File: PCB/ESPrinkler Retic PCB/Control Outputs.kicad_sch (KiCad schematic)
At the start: 117 parts, among them Q10 AO3400A, Q11 AO3400A, Q3 AO3400A, Q4 AO3400A, Q5 AO3400A, Q6 AO3400A, Q7 AO3400A, Q8 AO3400A, Q9 AO3400A, U10 MOC3063S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

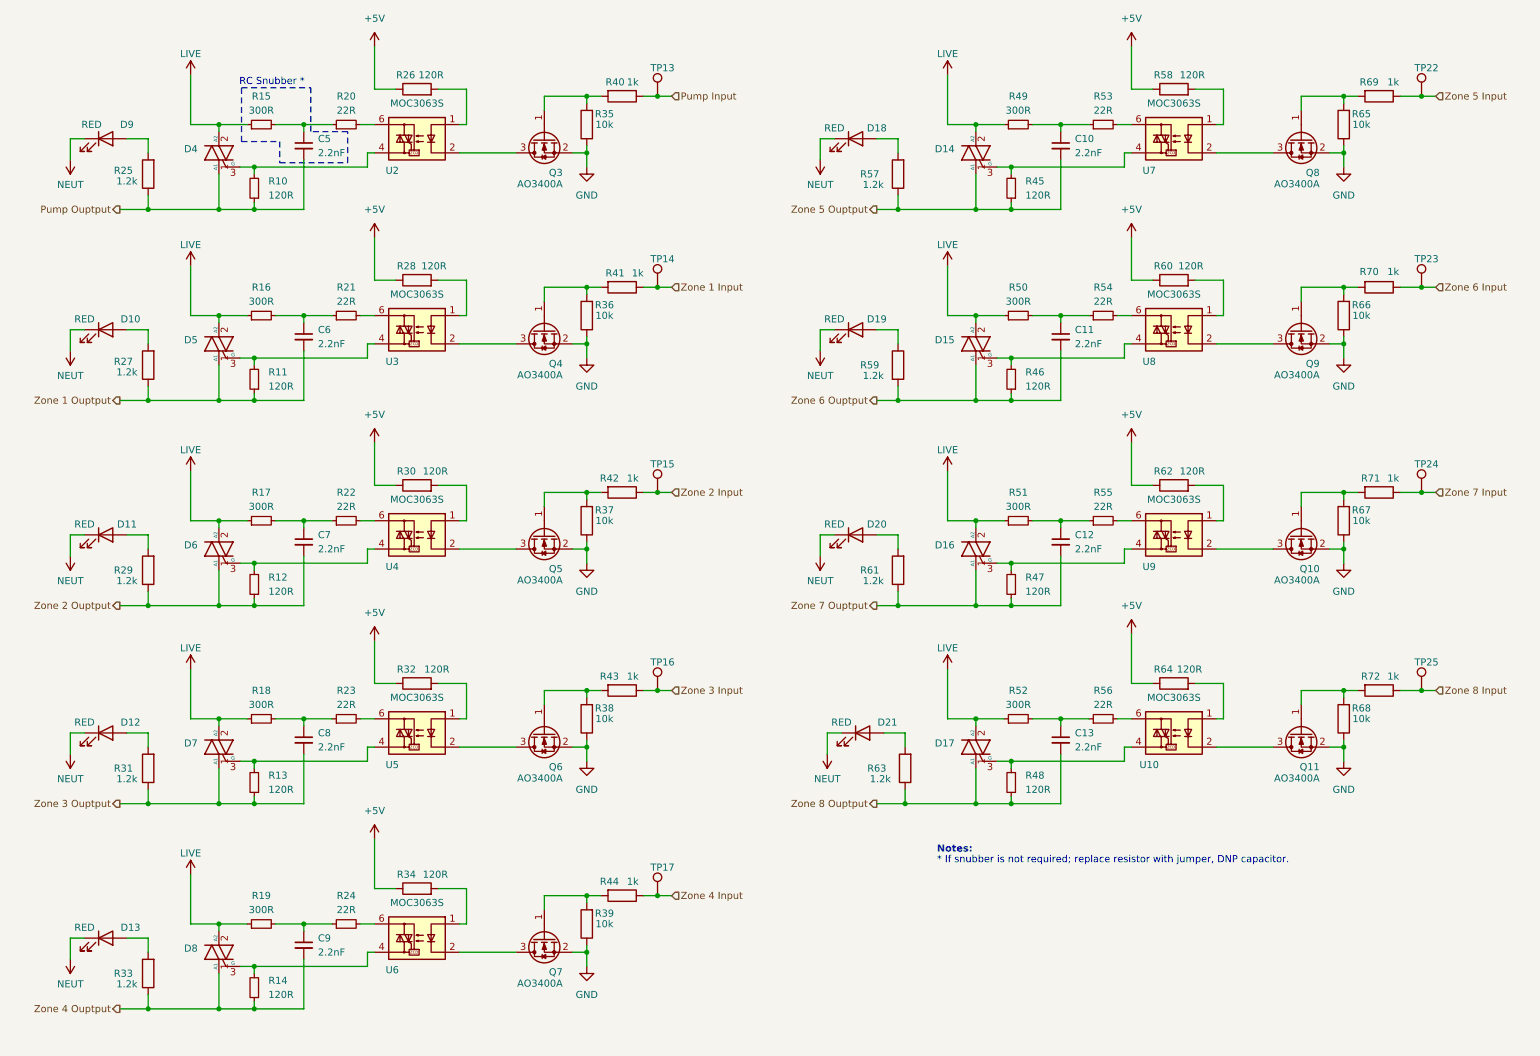
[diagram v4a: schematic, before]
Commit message: PCB version 1.1 following peer review
PTC in line with live, previously shorted between live and neutral.
Added boxes around sections on schematic for better readability.
Modified terminal block silkscreen to make more sense
Modified routing of 5V power to to reduce tunnels and traces on bottom plane.
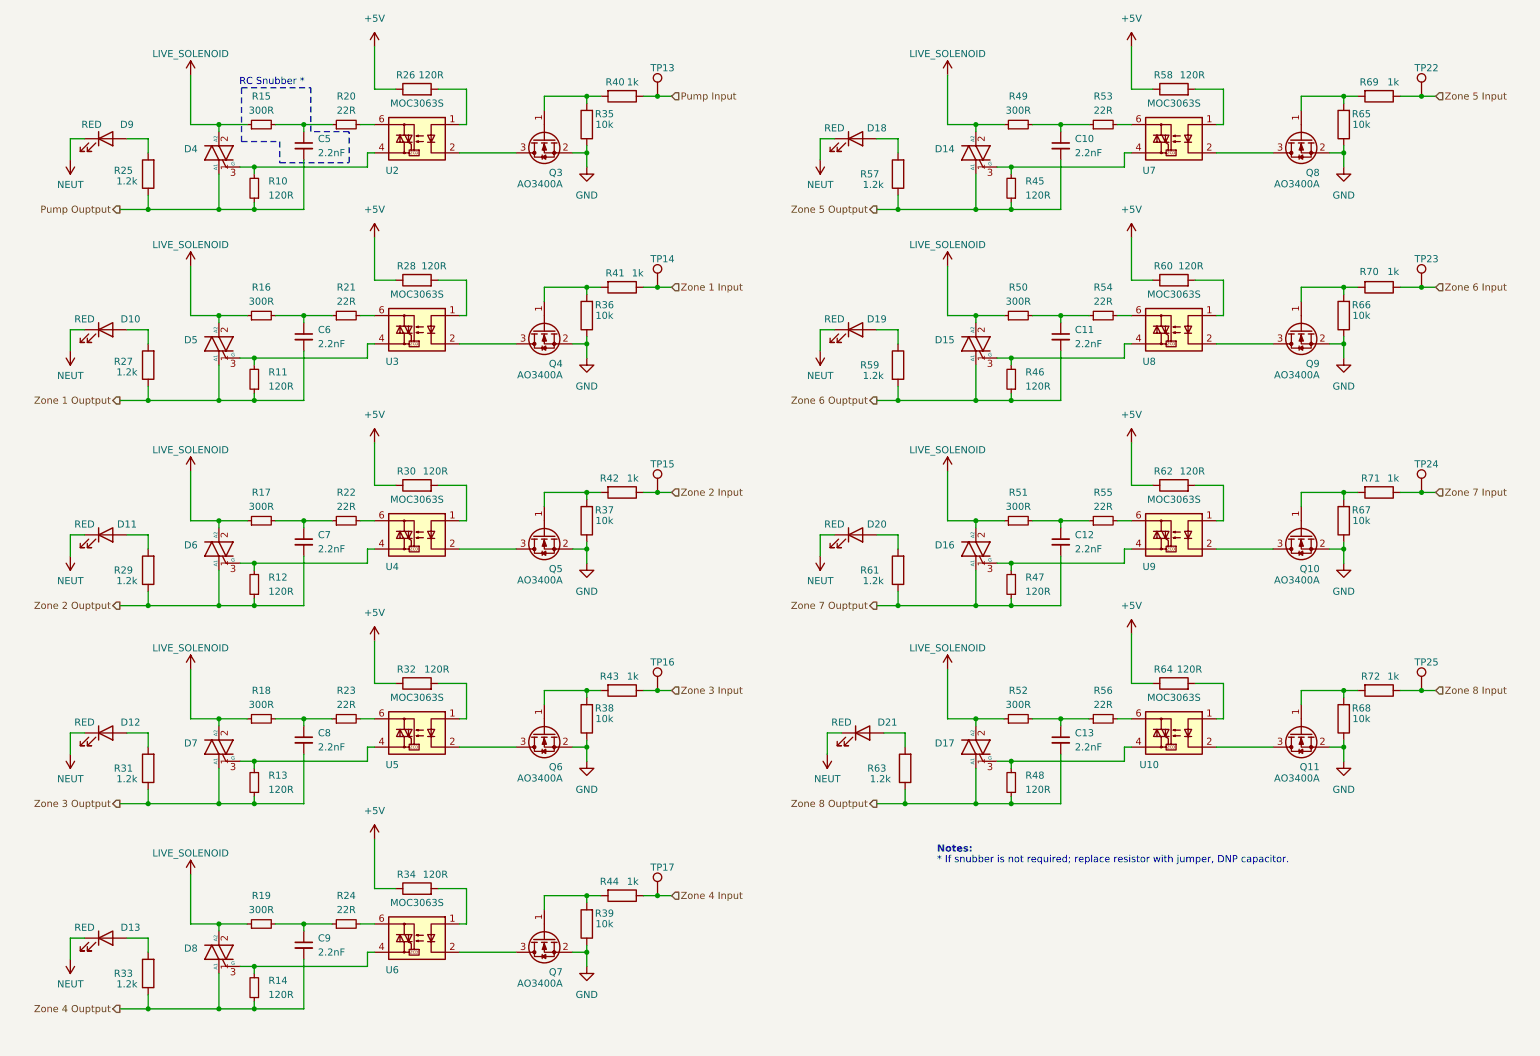
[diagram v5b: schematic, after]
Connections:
- net LIVE renamed LIVE_SOLENOID

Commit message: Continue V1.1 modifications
Round off corners on PCB
Remove solder mount for triacs, unnecessary addition. Can use adhesive if required to secure triacs.
Remove unnecessary vias between top and bottom ground planes
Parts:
- D14, D15, D16, D17, D4, D5, D6, D7, D8: footprint Footprints:TO-220-3_Horizontal_TabDown_Solder -> Footprints:TO-220-3_Horizontal_TabDown_NoHole
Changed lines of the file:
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@@
 			)
 		)
-		(property "Footprint" "Footprints:TO-220-3_Horizontal_TabDown_Solder"
+		(property "Footprint" "Footprints:TO-220-3_Horizontal_TabDown_NoHole"
 			(at 182.245 71.755 90)
 			(effects
@@
 			)
 		)
-		(property "Footprint" "Footprints:TO-220-3_Horizontal_TabDown_Solder"
+		(property "Footprint" "Footprints:TO-220-3_Horizontal_TabDown_NoHole"
 			(at 182.245 108.585 90)
 			(effects
@@
 			)
 		)
-		(property "Footprint" "Footprints:TO-220-3_Horizontal_TabDown_Solder"
+		(property "Footprint" "Footprints:TO-220-3_Horizontal_TabDown_NoHole"
 			(at 46.355 108.585 90)
 			(effects
@@
 			)
 		)
-		(property "Footprint" "Footprints:TO-220-3_Horizontal_TabDown_Solder"
+		(property "Footprint" "Footprints:TO-220-3_Horizontal_TabDown_NoHole"
 			(at 46.355 71.755 90)
 			(effects
@@
 			)
 		)
-		(property "Footprint" "Footprints:TO-220-3_Horizontal_TabDown_Solder"
+		(property "Footprint" "Footprints:TO-220-3_Horizontal_TabDown_NoHole"
 			(at 46.355 37.465 90)
 			(effects
@@
 			)
 		)
-		(property "Footprint" "Footprints:TO-220-3_Horizontal_TabDown_Solder"
+		(property "Footprint" "Footprints:TO-220-3_Horizontal_TabDown_NoHole"
 			(at 46.355 144.145 90)
 			(effects
@@
 			)
 		)
-		(property "Footprint" "Footprints:TO-220-3_Horizontal_TabDown_Solder"
+		(property "Footprint" "Footprints:TO-220-3_Horizontal_TabDown_NoHole"
 			(at 46.355 180.975 90)
 			(effects
@@
 			)
 		)
-		(property "Footprint" "Footprints:TO-220-3_Horizontal_TabDown_Solder"
+		(property "Footprint" "Footprints:TO-220-3_Horizontal_TabDown_NoHole"
 			(at 182.245 144.145 90)
 			(effects
@@
 			)
 		)
-		(property "Footprint" "Footprints:TO-220-3_Horizontal_TabDown_Solder"
+		(property "Footprint" "Footprints:TO-220-3_Horizontal_TabDown_NoHole"
 			(at 182.245 37.465 90)
 			(effects

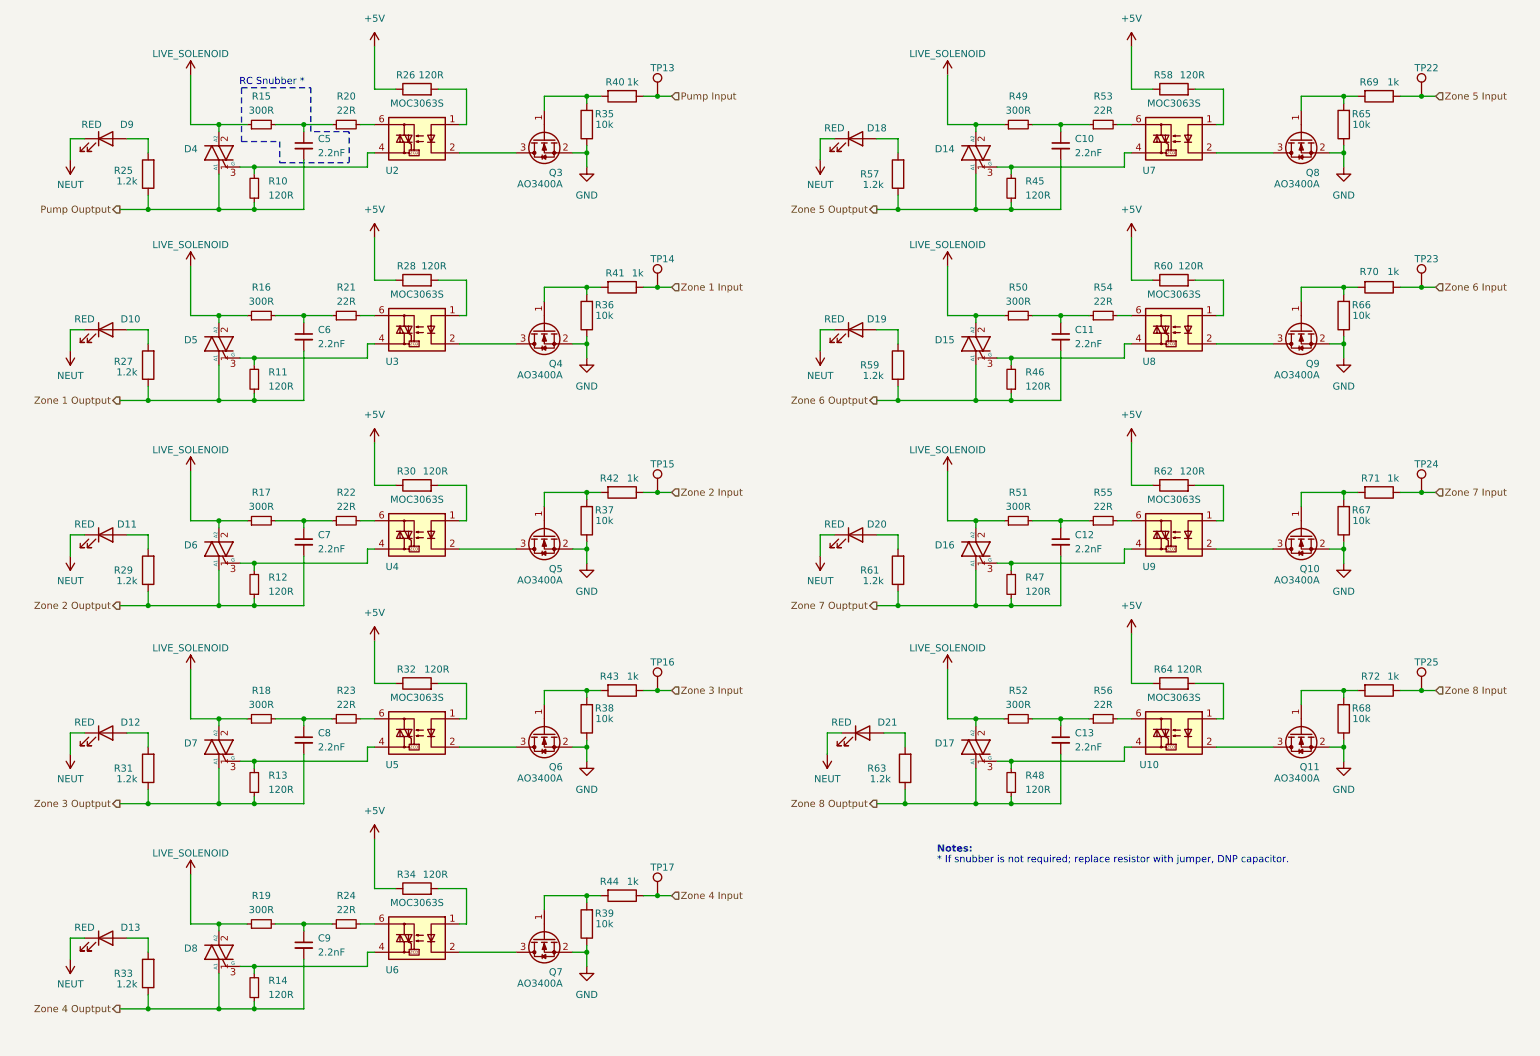
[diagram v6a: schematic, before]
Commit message: Update PCB and SCH for snubber circuit DNF
Snubber circuit is drawing too much power, capacitor and resistor values need to be looked at.
Not including the circuit for the time being.

Added alternate part for resistor, 0 ohm jumper.
DNF capacitor in snubber circuit for each output.
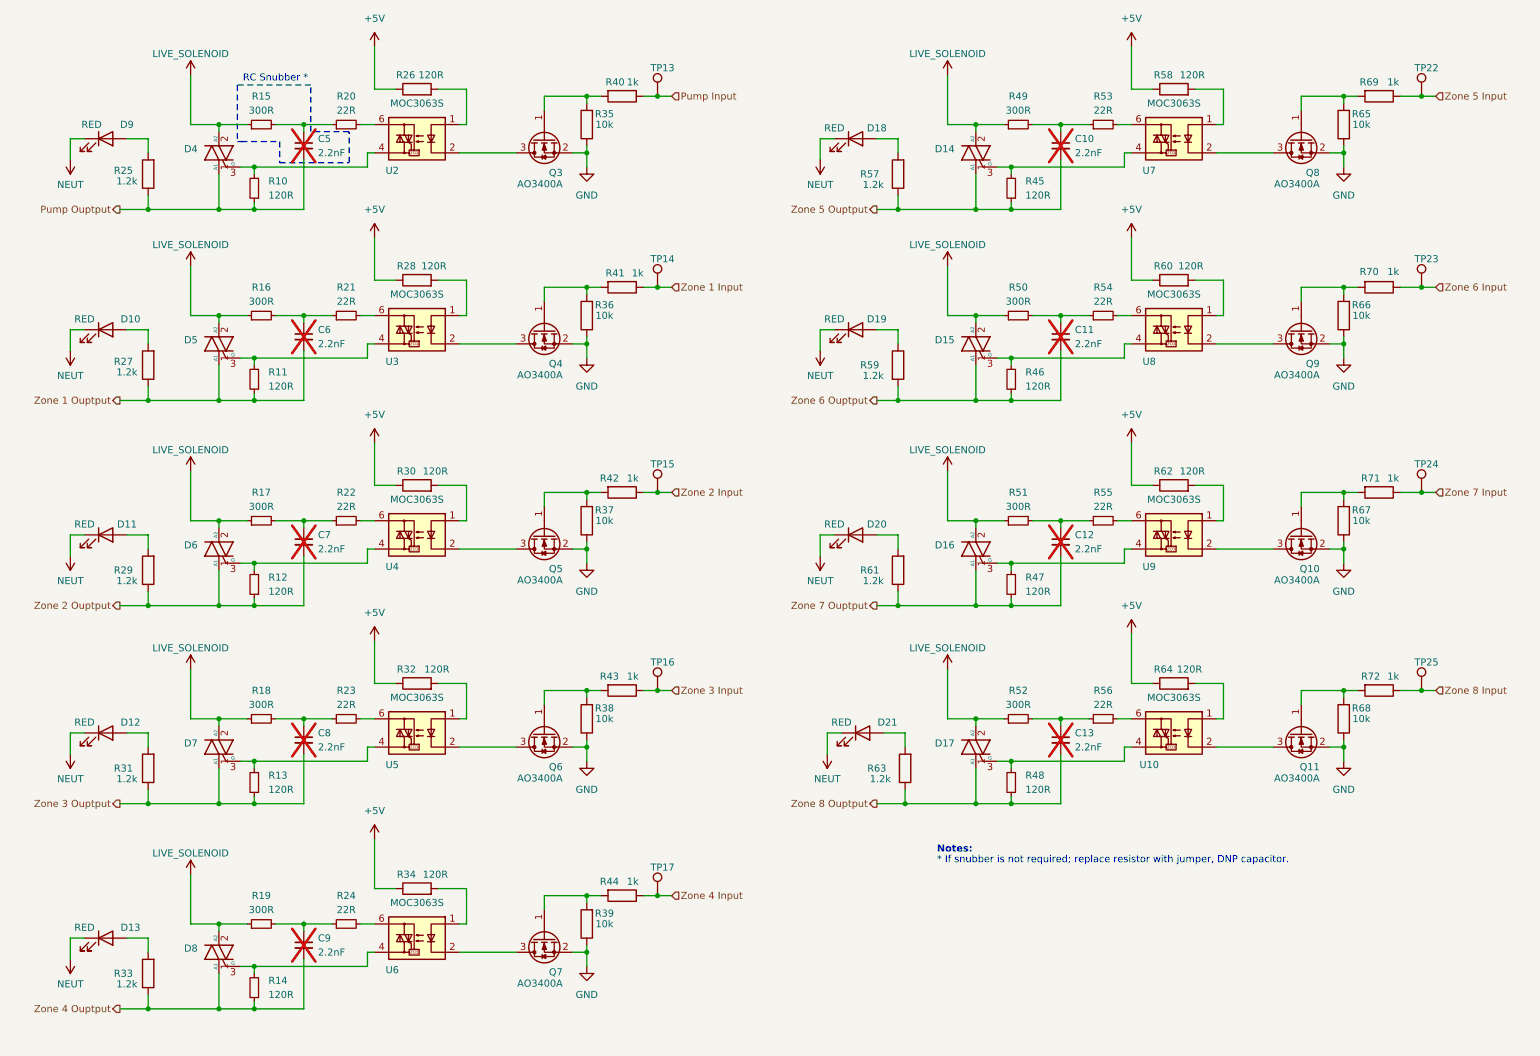
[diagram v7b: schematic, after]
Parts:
- C10, C11, C12, C13, C5, C6, C7, C8, C9: now not fitted
- R15, R16, R17, R18, R19, R49, R50, R51, R52: Alternate Manufacturer (none) -> UNI-ROYAL(Uniroyal Elec); Alternate Manufacturer P/N (none) -> 0805W8F0000T5E; Alternate Supplier (none) -> LCSC; Alternate Supplier P/N (none) -> C17477

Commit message: Remove snubber and bring Kicad V10 update
Remove snubber from triac driver as its not required.

Attempt to start migrating to Kicad V10
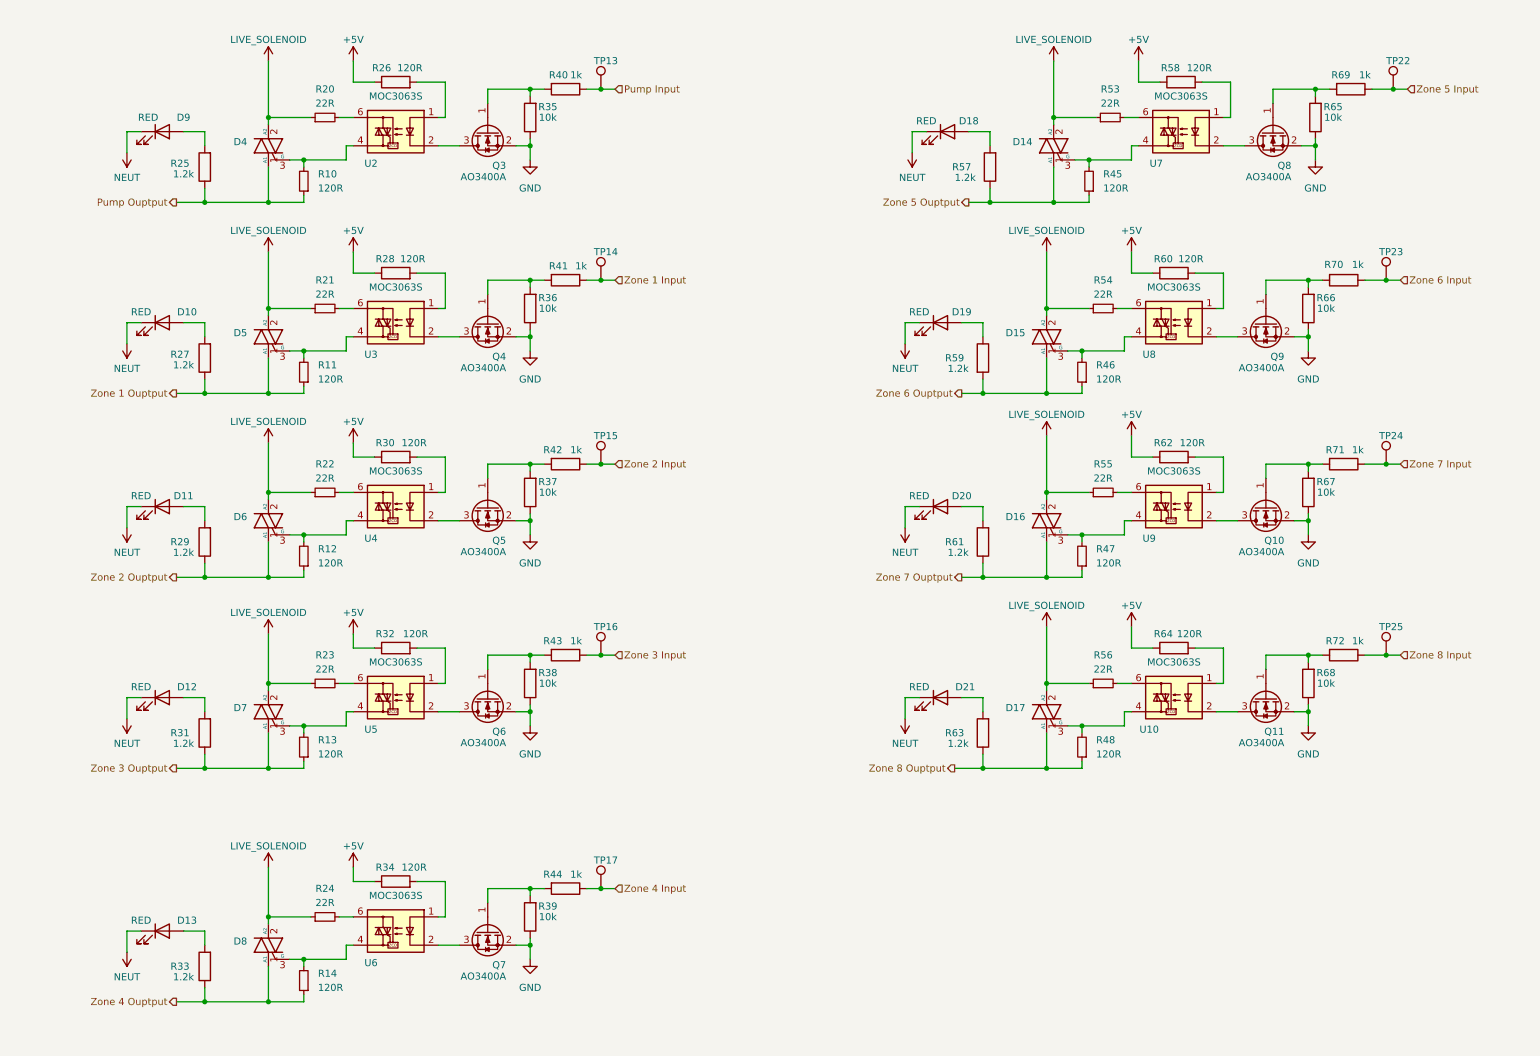
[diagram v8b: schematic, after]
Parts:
- removed C10, C11, C12, C13, C5, C6, C7, C8, C9: 2.2nF, Capacitor_SMD:C_0603_1608Metric, symbol Device:C_Small
- removed R15, R16, R17, R18, R19, R49, R50, R51, R52: 300R, Resistor_SMD:R_0805_2012Metric, symbol Device:R_Small
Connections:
- net LIVE_SOLENOID: now also R20.1, R21.1, R22.1, R23.1, R24.1, R53.1, R54.1, R55.1, R56.1
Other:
- note removed: "* If snubber is not required; replace resistor with jumper, DNP capacitor."
- note removed: "Notes:"
- note removed: "RC Snubber *"
- moved on the sheet: D10, D11, D12, D13, D14, D15, D16, D17, D18, D19, D20, D21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
